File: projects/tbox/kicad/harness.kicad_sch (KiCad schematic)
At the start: 0 parts

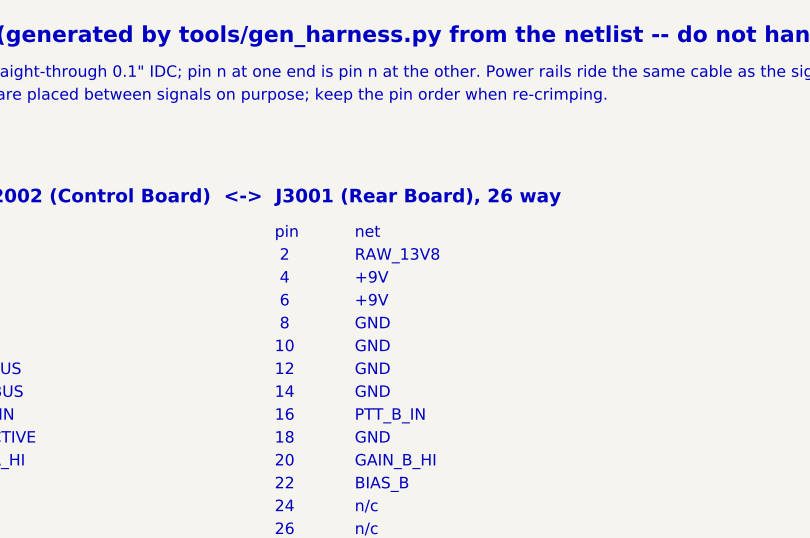
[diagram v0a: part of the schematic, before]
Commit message: Supply moves to the control board; rear board deepened to 90 mm
The rear board was 2.7x denser than the control board and nothing tied
the supply to the rear panel once the Powerpole became a pigtail.  The
Supply sheet now sits under the Control Board sheet (page 25, refs
31xx -> 25xx by table, mentions renamed the same way); the pigtail
lands on the control board's JST; BIAS_5V takes ribbon pin 2 (the bias
switches stay on the rear) and RAW_13V8 leaves the ribbon.  Netlist
otherwise identical.  Panel is now 300 x 270 (REAR 90 deep); harness
and power tree regenerated; drawings and DESIGN updated.

The PCB still holds the supply footprints under their old paths: next
Update PCB from Schematic re-links them, then place_panel --all.
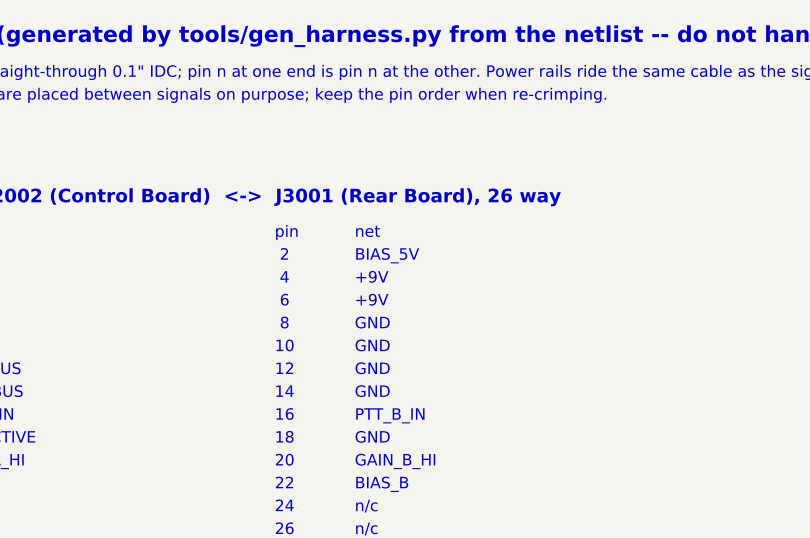
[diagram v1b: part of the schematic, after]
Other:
- note added: "BIAS_5V"
- note removed: "RAW_13V8"
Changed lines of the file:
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@@
   (text "GND" (exclude_from_sim no) (at 29.21 44.45 0) (effects (font (size 1.27 1.27)) (justify left bottom)))
   (text " 2" (exclude_from_sim no) (at 66.04 44.45 0) (effects (font (size 1.27 1.27)) (justify left bottom)))
-  (text "RAW_13V8" (exclude_from_sim no) (at 74.93 44.45 0) (effects (font (size 1.27 1.27)) (justify left bottom)))
+  (text "BIAS_5V" (exclude_from_sim no) (at 74.93 44.45 0) (effects (font (size 1.27 1.27)) (justify left bottom)))
   (text " 3" (exclude_from_sim no) (at 20.32 46.99 0) (effects (font (size 1.27 1.27)) (justify left bottom)))
   (text "GND" (exclude_from_sim no) (at 29.21 46.99 0) (effects (font (size 1.27 1.27)) (justify left bottom)))
